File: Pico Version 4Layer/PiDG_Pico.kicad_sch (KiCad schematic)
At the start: 46 parts, among them J1 Conn_02x05_Odd_Even, J10 Trig, J11 Laser Enable, J12 Pixel Reset, J14 Pico Socket A, J15 Pico Socket B, J16 Laser En/PWM Trig/GND, J2 Conn_02x05_Odd_Even, J3 Conn_02x05_Odd_Even, J4 Conn_02x05_Odd_Even, J5 Conn_02x05_Odd_Even, J6 Conn_02x05_Odd_Even, J7 Laser 1, J8 Laser 2, U1 74LVC1G04, U10 74AHCT1G08, U11 Raspberry Pi Pico 2 W, U12 74LVC1G17, U13 UCC27524, U2 SN74LVC04AD, U3 74LVC1G04, U4 SN74LVC04AD, U5 74LVC1G04, U6 SN74LVC04AD, U7 74AHCT1G08, U8 74AHCT1G08, U9 NCP718xSN180

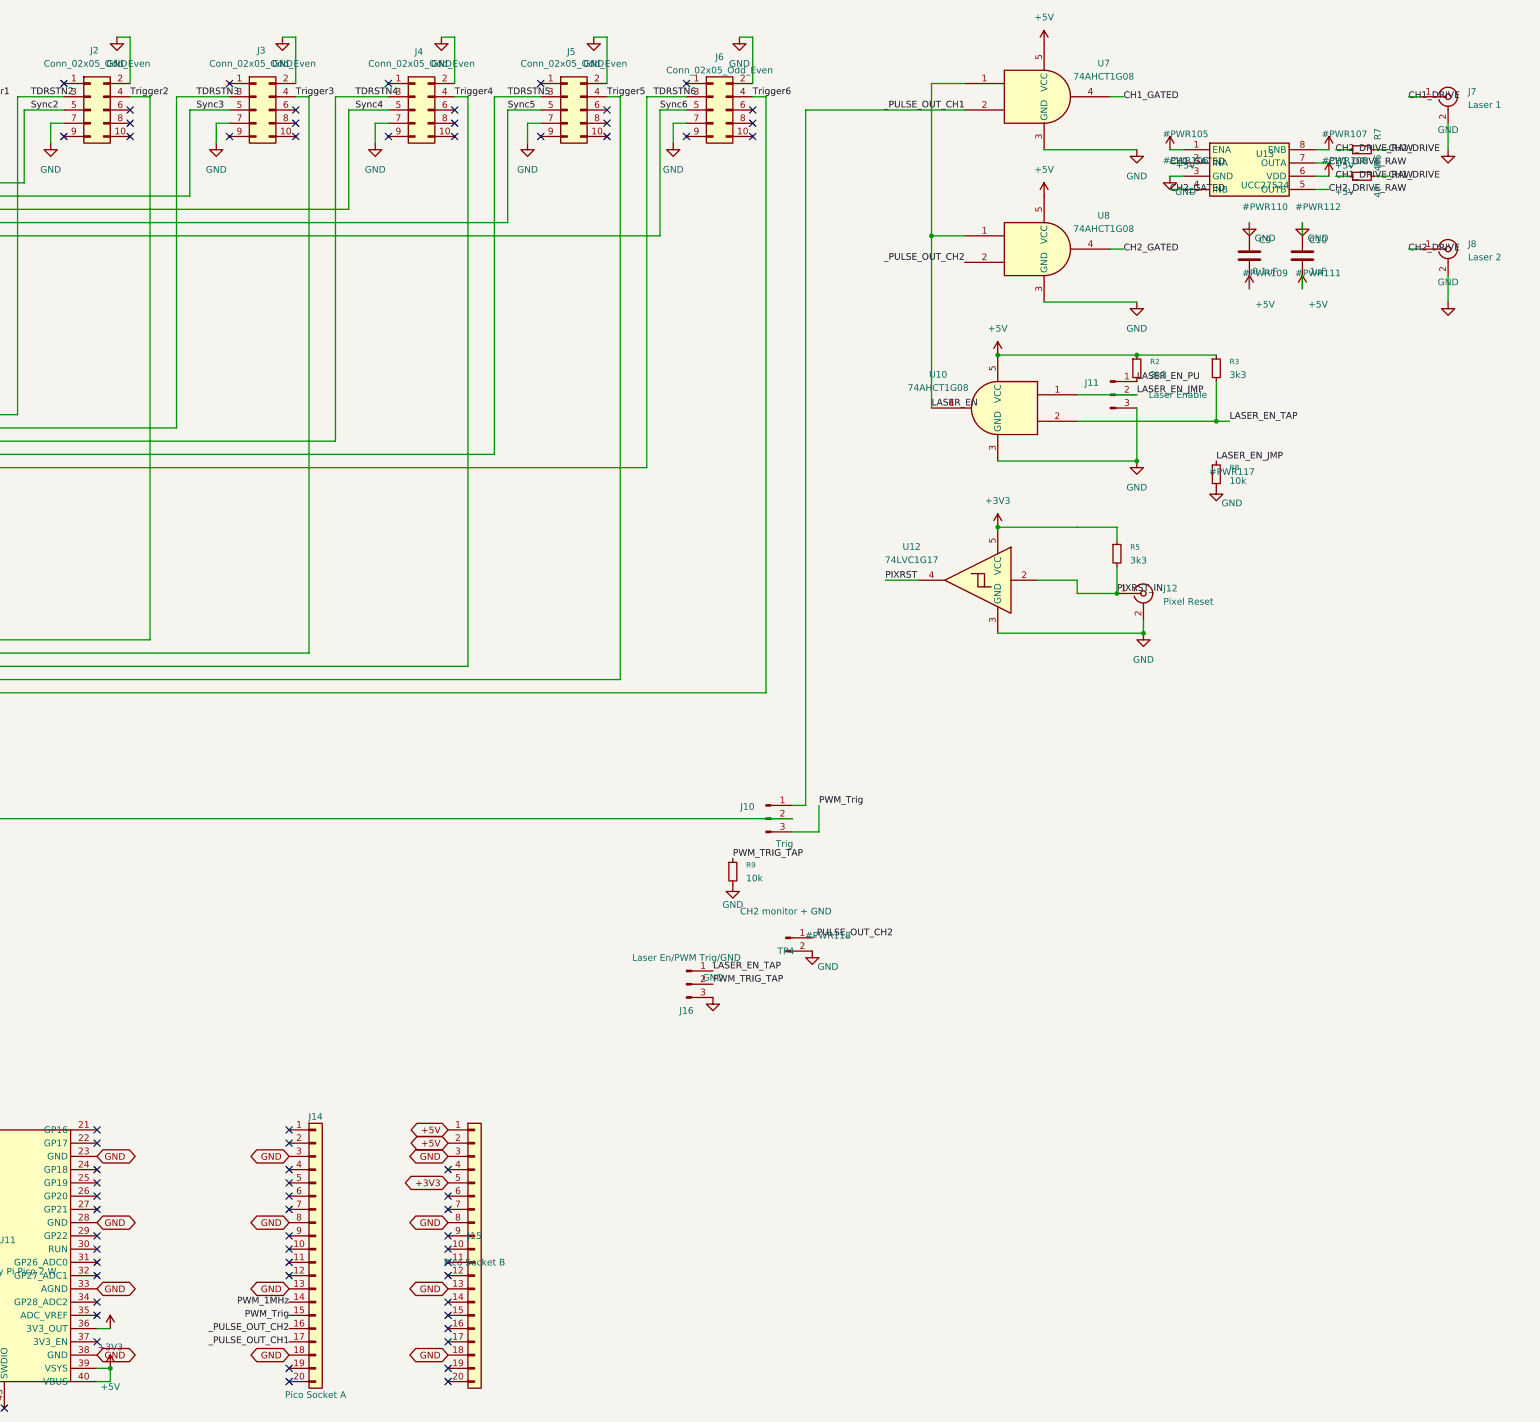
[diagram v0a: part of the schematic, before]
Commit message: USB-C PD power input: 12 V laser-driver rail and 5 V into the VSYS plane
J17 (USB-C, power only) + U14 CH224K request 15 V from a PD charger.
- U15 AP63205WU buck + U16 LM66100 ideal diode feed the +5V plane (Pico
  VSYS). CE tied to VOUT for reverse blocking.
- U17 LP2951 (adjustable, R12/R13 100k/11.3k 0.1 %) makes 12.0 V for the
  UCC27524. R14 1R gives the output ESR both TI LP2951 dies need.
- U17 ~ERROR drives U13 ENA/ENB (LASER_PWR_OK, R16 pull-up): outputs are
  held low with no PD, before the contract, and on 5 V/9 V chargers.
- R6/R7 47 -> 69.8 ohm: worst-case 4.55-5.16 V into the 50 ohm LDP-V
  trigger input (was ~2.4 V). C10 -> 10 uF 1206 on +12V.
- Pico VBUS (J15.1) disconnected from +5V; USB now reaches VSYS only
  through the Pico's own Schottky, so J17 cannot back-feed the host.
- R17/R18 10k pull-downs on the laser pulse nets: J17 can now power the
  board with the Pico removed.

ERC 0, DRC 0, 0 unconnected; 323 pads match the schematic netlist.
BOM/CPL regenerated (the CPL also picks up the AHCT values it had missed),
fab outputs regenerated, Hardware.md updated.

Co-Authored-By: Claude Opus 5.5 (1M context) <noreply@anthropic.com>
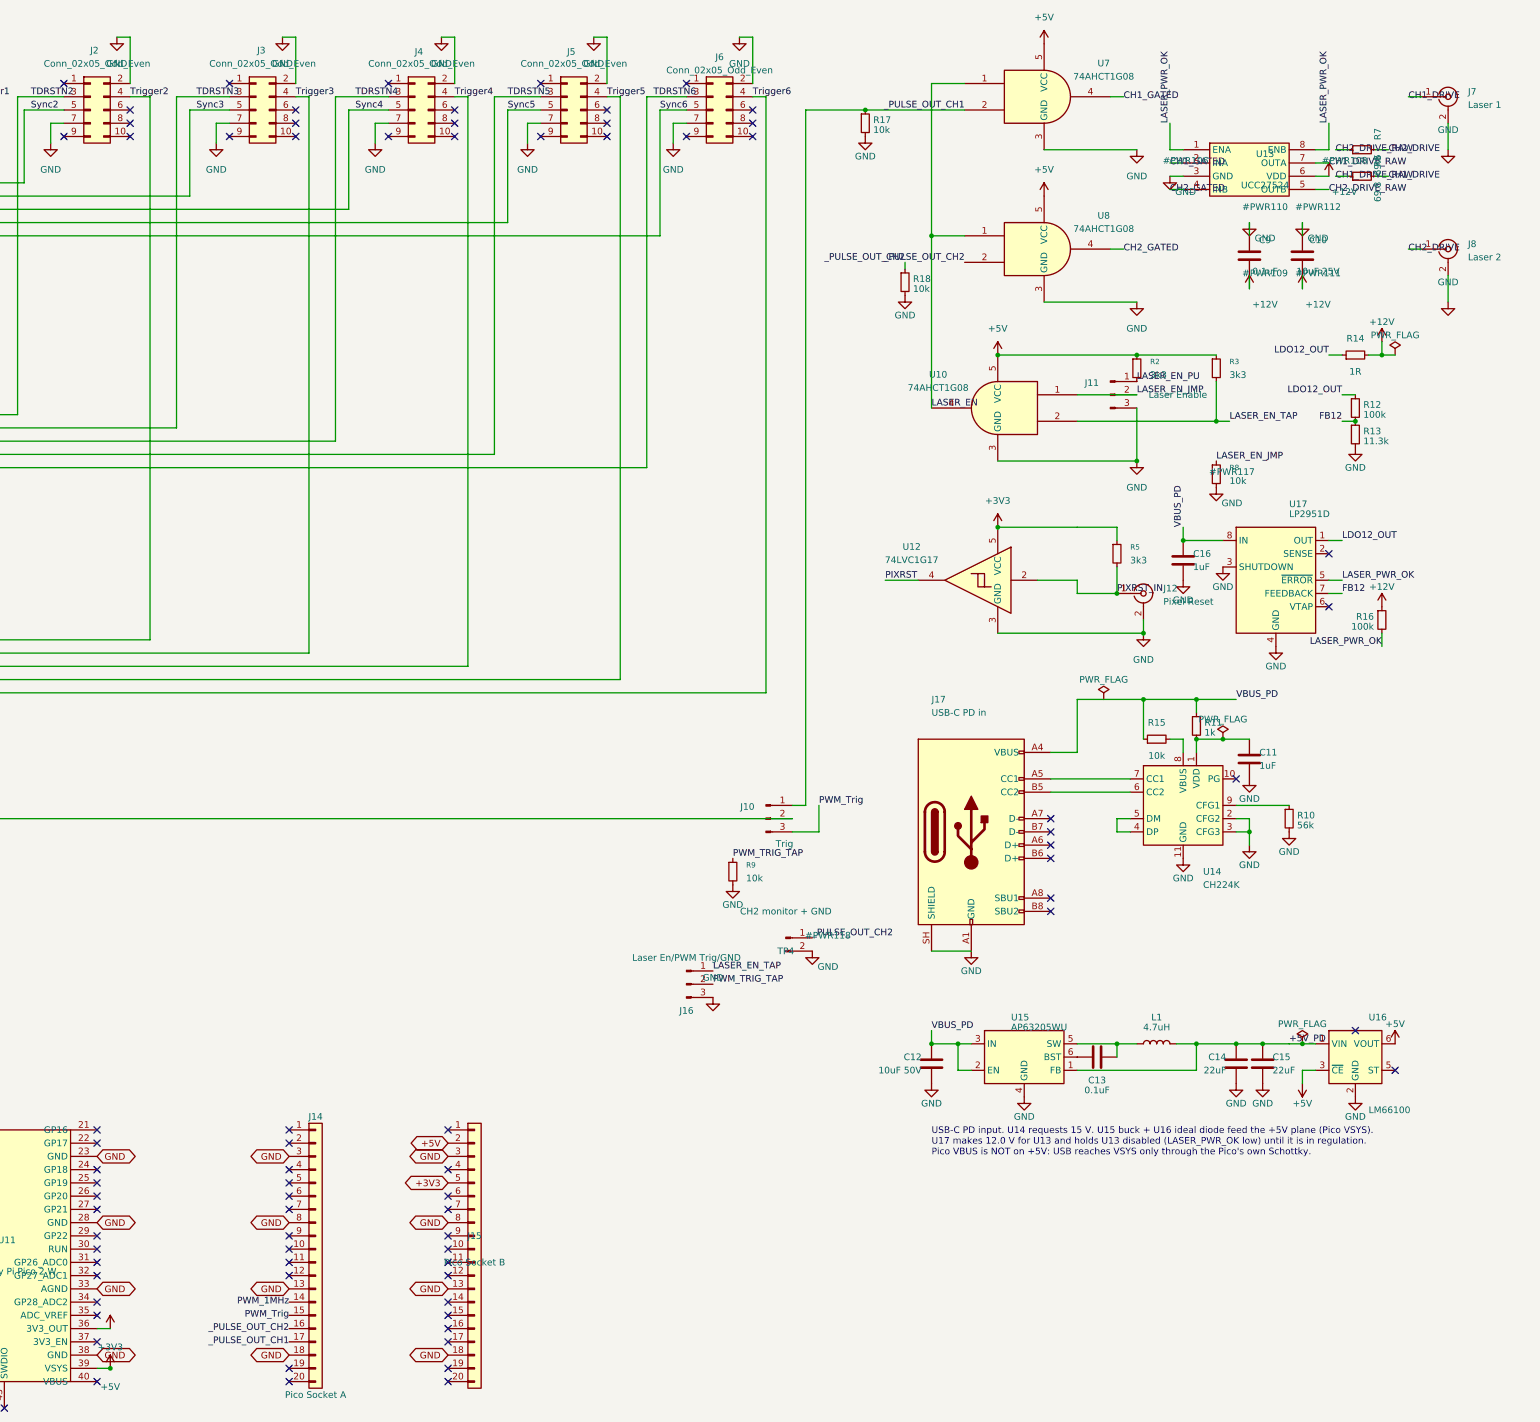
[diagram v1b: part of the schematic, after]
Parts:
- added C11, C16: 1uF, Capacitor_SMD:C_0805_2012Metric_Pad1.18x1.45mm_HandSolder, symbol Device:C
- added C12: 10uF 50V, Capacitor_SMD:C_1206_3216Metric_Pad1.33x1.80mm_HandSolder, symbol Device:C
- added C13: 0.1uF, Capacitor_SMD:C_0805_2012Metric_Pad1.18x1.45mm_HandSolder, symbol Device:C
- added C14, C15: 22uF, Capacitor_SMD:C_0805_2012Metric_Pad1.18x1.45mm_HandSolder, symbol Device:C
- added J17: USB-C PD in, PiDG_Local:USB_C_Receptacle_HRO_TYPE-C-31-M-12_EdgeTrim, symbol Connector:USB_C_Receptacle_USB2.0_16P
- added L1: 4.7uH, Inductor_SMD:L_Cenker_CKCS4030, symbol Device:L
- added R10: 56k, Resistor_SMD:R_0805_2012Metric_Pad1.20x1.40mm_HandSolder, symbol Device:R_Small
- added R11: 1k, Resistor_SMD:R_1206_3216Metric_Pad1.30x1.75mm_HandSolder, symbol Device:R_Small
- added R12, R16: 100k, Resistor_SMD:R_0805_2012Metric_Pad1.20x1.40mm_HandSolder, symbol Device:R_Small
- added R13: 11.3k, Resistor_SMD:R_0805_2012Metric_Pad1.20x1.40mm_HandSolder, symbol Device:R_Small
- added R14: 1R, Resistor_SMD:R_0805_2012Metric_Pad1.20x1.40mm_HandSolder, symbol Device:R_Small
- added R15, R17, R18: 10k, Resistor_SMD:R_0805_2012Metric_Pad1.20x1.40mm_HandSolder, symbol Device:R_Small
- added U14: CH224K, Package_SO:SSOP-10-1EP_3.9x4.9mm_P1mm_EP2.1x3.3mm, symbol Interface_USB:CH224K
- added U15: AP63205WU, Package_TO_SOT_SMD:TSOT-23-6_HandSoldering, symbol Regulator_Switching:AP63205WU
- added U16: LM66100, Package_TO_SOT_SMD:SOT-363_SC-70-6, symbol Power_Management:LM66100DCK
- added U17: LP2951D, Package_SO:SOIC-8_3.9x4.9mm_P1.27mm, symbol Regulator_Linear:LP2951-3.0_SOIC
- C10: value 1uF -> 10uF 25V; footprint Capacitor_SMD:C_0805_2012Metric_Pad1.18x1.45mm_HandSolder -> Capacitor_SMD:C_1206_3216Metric_Pad1.33x1.80mm_HandSolder
- R6, R7: value 47 -> 69.8
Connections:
- net +5V: now also U16.3 (~{CE}), U16.6 (VOUT); no longer C10.2, C9.2, J15.1 (Pin_1), U11.40 (VBUS), U13.1 (ENA), U13.6 (VDD), U13.8 (ENB)
- net GND: now also C11.2, C12.2, C14.2, C15.2, C16.2, J17.A1 (GND), J17.A12 (GND), J17.B1 (GND), J17.B12 (GND), J17.SH (SHIELD), R10.2, R13.2, R17.2, R18.2, U14.11 (GND), U14.2 (CFG2), U14.3 (CFG3), U15.4 (GND), U16.2 (GND), U17.3 (SHUTDOWN), U17.4 (GND)
- net _PULSE_OUT_CH1: now also R17.1
- net _PULSE_OUT_CH2: now also R18.1
- new net: C13.2, L1.1, U15.5 (SW)
- new net: R15.2, U14.8 (VBUS)
- new net: C11.1, R11.2, U14.1 (VDD)
- new net: U14.4 (DP), U14.5 (DM)
- new net: J17.B5 (CC2), U14.6 (CC2)
- new net: J17.A5 (CC1), U14.7 (CC1)
- new net: R10.1, U14.9 (CFG1)
- new net: C13.1, U15.6 (BST)
- new net +12V: C10.2, C9.2, R14.2, R16.1, U13.6 (VDD)
- new net +5V_PD: C14.1, C15.1, L1.2, U15.1 (FB), U16.1 (VIN)
- new net FB12: R12.2, R13.1, U17.7 (FEEDBACK)
- new net LASER_PWR_OK: R16.2, U13.1 (ENA), U13.8 (ENB), U17.5 (~{ERROR})
- new net LDO12_OUT: R12.1, R14.1, U17.1 (OUT)
- new net VBUS_PD: C12.1, C16.1, J17.A4 (VBUS), J17.A9 (VBUS), J17.B4 (VBUS), J17.B9 (VBUS), R11.1, R15.1, U15.2 (EN), U15.3 (IN), U17.8 (IN)
- no-connect marks 83 -> 96
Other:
- note added: "USB-C PD input. U14 requests 15 V. U15 buck + U16 ideal diode feed the +5V plane (Pico VSYS). U17 makes 12.0 V for U13 and holds U13 disabled (LASER_PWR_OK low) until it is in regulation. Pico VBUS is NOT on +5V: USB reaches VSYS only through the Pico's own Schottky."
